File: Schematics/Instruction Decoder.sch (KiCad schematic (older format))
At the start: 0 parts

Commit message: Flesh out the Instruction Decoder.
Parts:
- added C? (x7): 100nF, symbol Device:C
- added U? (x2): GLS29EE010, symbol Memory_EEPROM:GLS29EE010
- added U? (x3): 74F574, symbol 74xx:74LS574
- added U?: 74LS245, symbol 74xx:74LS245
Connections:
- new net: U?.13 (DQ0), U?.2 (D0) (x2)
- new net: U?.14 (DQ1), U?.3 (D1) (x2)
- new net: U?.15 (DQ2), U?.4 (D2) (x2)
- new net: U?.17 (DQ3), U?.5 (D3) (x2)
- new net: U?.18 (DQ4), U?.6 (D4) (x2)
- new net: U?.19 (DQ5), U?.7 (D5) (x2)
- new net: U?.20 (DQ6), U?.8 (D6) (x2)
- new net: U?.21 (DQ7), U?.9 (D7) (x2)
- new net: U?.12 (Q7), U?.9 (A7)
- new net: U?.13 (Q6), U?.8 (A6)
- new net: U?.14 (Q5), U?.7 (A5)
- new net: U?.15 (Q4), U?.6 (A4)
- new net: U?.16 (Q3), U?.5 (A3)
- new net: U?.17 (Q2), U?.4 (A2)
- new net: U?.18 (Q1), U?.3 (A1)
- new net: U?.19 (Q0), U?.2 (A0)
- new net ControlClock: U?.11 (Cp), U?.11 (Cp), U?.11 (Cp)
- new net DataBus0: U?.18 (B0)
- new net DataBus1: U?.17 (B1)
- new net DataBus2: U?.16 (B2)
- new net DataBus3: U?.15 (B3)
- new net DataBus4: U?.14 (B4)
- new net DataBus5: U?.13 (B5)
- new net DataBus6: U?.12 (B6)
- new net DataBus7: U?.11 (B7)
- new net GND: C?.2, C?.2, C?.2, C?.2, C?.2, C?.2, C?.2, U?.1 (OE), U?.1 (OE), U?.1 (OE), U?.10 (GND), U?.10 (GND), U?.10 (GND), U?.10 (GND), U?.16 (VSS), U?.16 (VSS), U?.2 (A16), U?.2 (A16), U?.22 (CE), U?.22 (CE), U?.23 (A10), U?.23 (A10), U?.24 (OE), U?.24 (OE), U?.25 (A11), U?.25 (A11), U?.28 (A13), U?.28 (A13), U?.29 (A14), U?.29 (A14), U?.3 (A15), U?.3 (A15), U?.4 (A12), U?.4 (A12)
- new net IR00: U?.2 (D0)
- new net IR01: U?.3 (D1)
- new net IR02: U?.4 (D2)
- new net IR03: U?.5 (D3)
- new net IR04: U?.6 (D4)
- new net IR05: U?.7 (D5)
- new net IR06: U?.8 (D6)
- new net IR07: U?.9 (D7)
- new net IR08: U?.12 (A0), U?.12 (A0)
- new net IR09: U?.11 (A1), U?.11 (A1)
- new net IR10: U?.10 (A2), U?.10 (A2)
- new net IR11: U?.9 (A3), U?.9 (A3)
- new net IR12: U?.8 (A4), U?.8 (A4)
- new net IR13: U?.7 (A5), U?.7 (A5)
- new net IR14: U?.6 (A6), U?.6 (A6)
- new net IR15: U?.5 (A7), U?.5 (A7)
- new net VCC: C?.1, C?.1, C?.1, C?.1, C?.1, C?.1, C?.1, U?.1 (A->B), U?.20 (VCC), U?.20 (VCC), U?.20 (VCC), U?.20 (VCC), U?.31 (WE), U?.31 (WE), U?.32 (VDD), U?.32 (VDD)
- new net ~A=B: U?.27 (A8), U?.27 (A8)
- new net ~CO: U?.19 (CE)
- new net ~CarryOut: U?.26 (A9), U?.26 (A9)
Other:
- note added: "The lower eight bits of the instruction\ncan be expressed onto the bus as a\nconstant value."

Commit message: Review decoupling capacitors again.
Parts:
- removed C?: 100nF, symbol Device:C
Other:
- note added: "ID/EX registers"
- note added: "Microcode ROMs"
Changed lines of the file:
@@
-	1    0    0    -1
-$EndComp
-$Comp
-L Device:C C?
-U 1 1 5DC6562A
-P 10150 950
-AR Path="/5D2C0761/5DC6562A" Ref="C?"  Part="1"
-AR Path="/5D2C0B92/5DC6562A" Ref="C?"  Part="1"
-F 0 "C?" H 10265 996 50  0000 L CNN
-F 1 "100nF" H 10265 905 50  0000 L CNN
-F 2 "" H 10188 800 50  0001 C CNN
-F 3 "~" H 10150 950 50  0001 C CNN
-	1    10150 950
 	1    0    0    -1
 $EndComp
@@
 	9150 800  9650 800
 Wire Wire Line
-	9650 800  10150 800
-Connection ~ 9650 800
-Wire Wire Line
-	10150 1100 9650 1100
-Wire Wire Line
 	9650 1100 9150 1100
-Connection ~ 9650 1100
 Connection ~ 9150 800
 Connection ~ 9150 1100
@@
 Text GLabel 9950 3000 2    50   Output ~ 0
 ControlWord
+Text Notes 6500 6350 0    50   ~ 0
+The lower eight bits of the instruction\ncan be expressed onto the bus as a\nconstant value.
 Wire Bus Line
 	6200 4550 6200 5250
@@
 Wire Bus Line
 	1850 1250 1850 7250
-Text Notes 6500 6350 0    50   ~ 0
-The lower eight bits of the instruction\ncan be expressed onto the bus as a\nconstant value.
+Text Notes 4150 650  0    50   ~ 0
+ID/EX registers
+Text Notes 2600 700  0    50   ~ 0
+Microcode ROMs
 $EndSCHEMATC

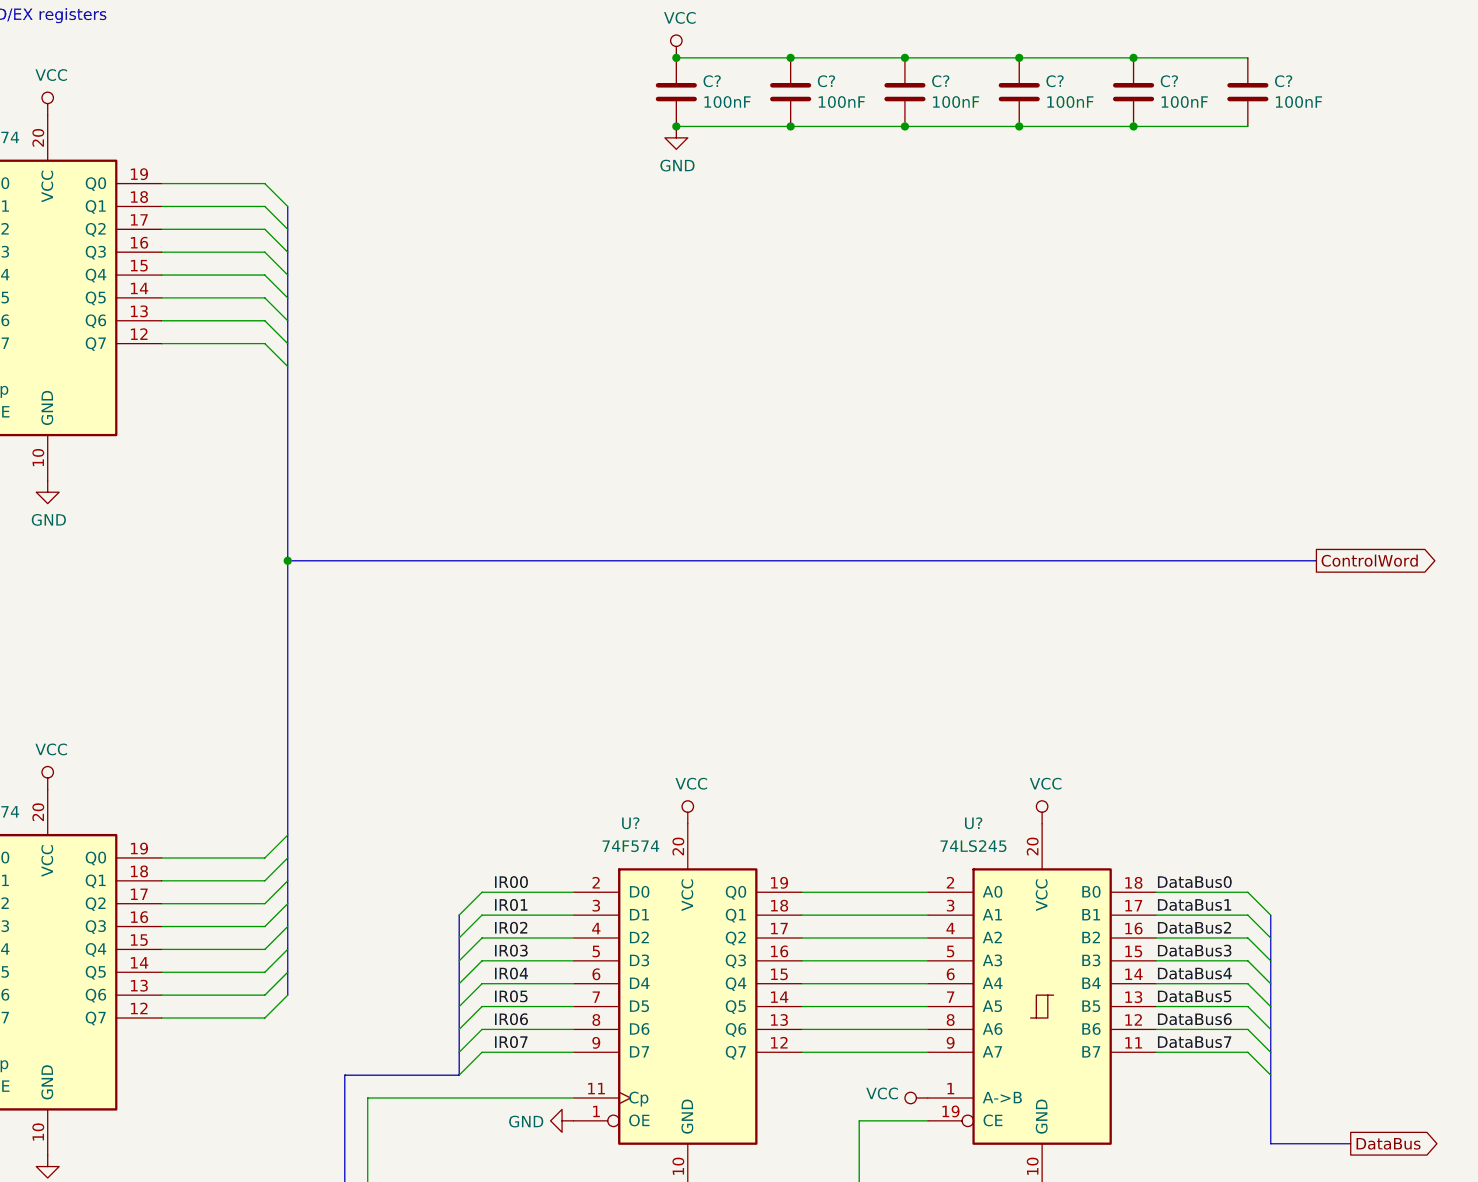
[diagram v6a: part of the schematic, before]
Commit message: Change net labels on buses to make them more consistent.
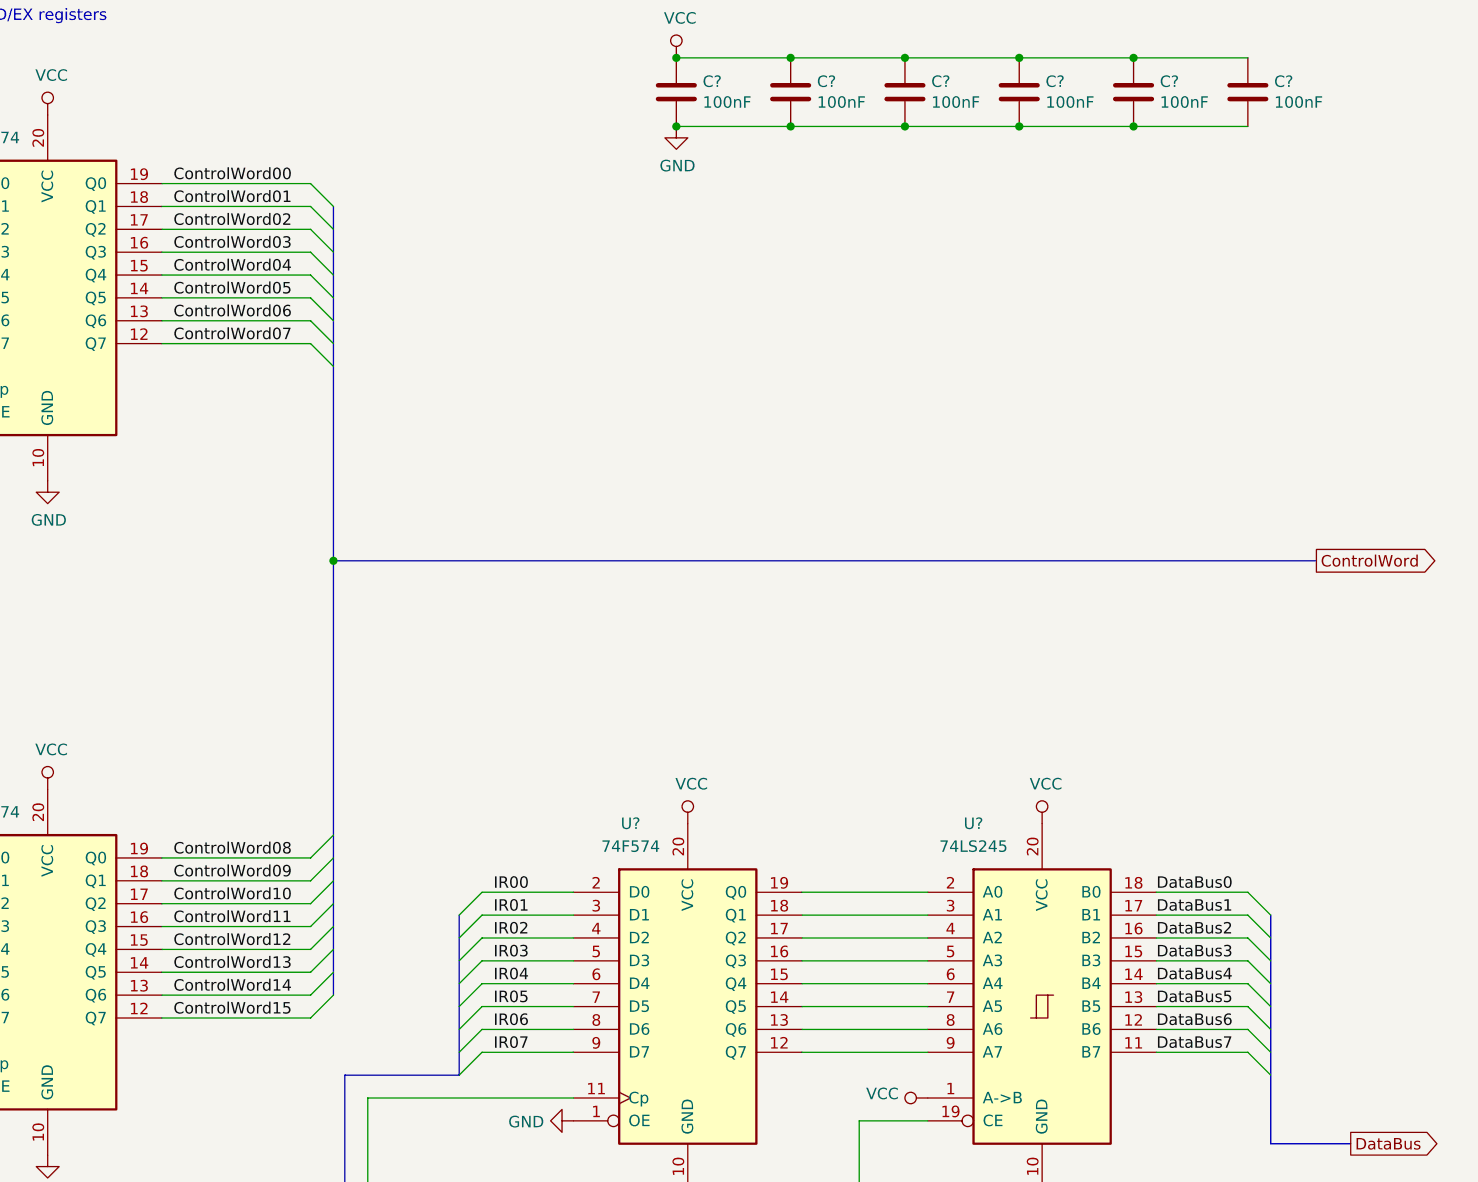
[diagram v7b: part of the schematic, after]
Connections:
- net ControlWord07: now reaches U?.12 (Q7)
- net ControlWord06: now reaches U?.13 (Q6)
- net ControlWord05: now reaches U?.14 (Q5)
- net ControlWord04: now reaches U?.15 (Q4)
- net ControlWord03: now reaches U?.16 (Q3)
- net ControlWord02: now reaches U?.17 (Q2)
- net ControlWord01: now reaches U?.18 (Q1)
- net ControlWord00: now reaches U?.19 (Q0)
- net ControlWord15: now reaches U?.12 (Q7)
- net ControlWord14: now reaches U?.13 (Q6)
- net ControlWord13: now reaches U?.14 (Q5)
- net ControlWord12: now reaches U?.15 (Q4)
- net ControlWord11: now reaches U?.16 (Q3)
- net ControlWord10: now reaches U?.17 (Q2)
- net ControlWord09: now reaches U?.18 (Q1)
- net ControlWord08: now reaches U?.19 (Q0)
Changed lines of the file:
@@
 $EndComp
 Entry Wire Line
-	5350 1350 5450 1450
+	5550 1350 5650 1450
 Entry Wire Line
-	5350 1450 5450 1550
+	5550 1450 5650 1550
 Entry Wire Line
-	5350 1550 5450 1650
+	5550 1550 5650 1650
 Entry Wire Line
-	5350 1650 5450 1750
+	5550 1650 5650 1750
 Entry Wire Line
-	5350 1750 5450 1850
+	5550 1750 5650 1850
 Entry Wire Line
-	5350 1850 5450 1950
+	5550 1850 5650 1950
 Entry Wire Line
-	5350 1950 5450 2050
+	5550 1950 5650 2050
 Entry Wire Line
-	5350 2050 5450 2150
+	5550 2050 5650 2150
 Entry Wire Line
-	5350 4300 5450 4200
+	5550 4300 5650 4200
 Entry Wire Line
-	5350 4400 5450 4300
+	5550 4400 5650 4300
 Entry Wire Line
-	5350 4500 5450 4400
+	5550 4500 5650 4400
 Entry Wire Line
-	5350 4600 5450 4500
+	5550 4600 5650 4500
 Entry Wire Line
-	5350 4700 5450 4600
+	5550 4700 5650 4600
 Entry Wire Line
-	5350 4800 5450 4700
+	5550 4800 5650 4700
 Entry Wire Line
-	5350 4900 5450 4800
+	5550 4900 5650 4800
 Entry Wire Line
-	5350 5000 5450 4900
+	5550 5000 5650 4900
 Wire Wire Line
-	5350 1350 4900 1350
+	5550 1350 4900 1350
 Wire Wire Line
-	4900 1450 5350 1450
+	4900 1450 5550 1450
 Wire Wire Line
-	5350 1550 4900 1550
+	5550 1550 4900 1550
 Wire Wire Line
-	4900 1650 5350 1650
+	4900 1650 5550 1650
 Wire Wire Line
-	5350 1750 4900 1750
+	5550 1750 4900 1750
 Wire Wire Line
-	4900 1850 5350 1850
+	4900 1850 5550 1850
 Wire Wire Line
-	5350 1950 4900 1950
+	5550 1950 4900 1950
 Wire Wire Line
-	4900 2050 5350 2050
+	4900 2050 5550 2050
 Wire Wire Line
-	5350 4300 4900 4300
+	5550 4900 4900 4900
 Wire Wire Line
-	4900 4400 5350 4400
-Wire Wire Line
-	5350 4500 4900 4500
-Wire Wire Line
-	4900 4600 5350 4600
-Wire Wire Line
-	5350 4700 4900 4700
-Wire Wire Line
-	4900 4800 5350 4800
-Wire Wire Line
-	5350 4900 4900 4900
-Wire Wire Line
-	4900 5000 5350 5000
+	4900 5000 5550 5000
 Wire Bus Line
-	5450 3000 9950 3000
-Connection ~ 5450 3000
+	5650 3000 9950 3000
+Connection ~ 5650 3000
 Text GLabel 9950 3000 2    50   Output ~ 0
 ControlWord
@@
 Text Notes 2600 700  0    50   ~ 0
 Microcode ROMs
+Text Label 4950 1350 0    50   ~ 0
+ControlWord00
+Text Label 4950 1450 0    50   ~ 0
+ControlWord01
+Text Label 4950 1550 0    50   ~ 0
+ControlWord02
+Text Label 4950 1650 0    50   ~ 0
+ControlWord03
+Text Label 4950 1750 0    50   ~ 0
+ControlWord04
+Text Label 4950 1850 0    50   ~ 0
+ControlWord05
+Text Label 4950 1950 0    50   ~ 0
+ControlWord06
+Text Label 4950 2050 0    50   ~ 0
+ControlWord07
+Wire Wire Line
+	4900 4800 5550 4800
+Wire Wire Line
+	4900 4700 5550 4700
+Wire Wire Line
+	4900 4600 5550 4600
+Wire Wire Line
+	4900 4500 5550 4500
+Wire Wire Line
+	4900 4400 5550 4400
+Wire Wire Line
+	4900 4300 5550 4300
 Wire Bus Line
 	6200 4550 6200 5250
 Wire Bus Line
+	5650 3000 5650 4900
+Wire Bus Line
 	9750 4550 9750 5550
 Wire Bus Line
-	5450 1450 5450 3000
-Wire Bus Line
-	5450 3000 5450 4900
+	5650 1450 5650 3000
 Wire Bus Line
 	1850 1250 1850 7250
+Text Label 4950 4300 0    50   ~ 0
+ControlWord08
+Text Label 4950 4400 0    50   ~ 0
+ControlWord09
+Text Label 4950 4500 0    50   ~ 0
+ControlWord10
+Text Label 4950 4600 0    50   ~ 0
+ControlWord11
+Text Label 4950 4700 0    50   ~ 0
+ControlWord12
+Text Label 4950 4800 0    50   ~ 0
+ControlWord13
+Text Label 4950 4900 0    50   ~ 0
+ControlWord14
+Text Label 4950 5000 0    50   ~ 0
+ControlWord15
 $EndSCHEMATC
